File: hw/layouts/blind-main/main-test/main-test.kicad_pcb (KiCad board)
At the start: 2 copper layers, 148 parts

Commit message: Integrate regenerative clamp, thermal inhibit and priced component capture
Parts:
- added C55: , SAMSUNG_CL05B104KB54PNC:C0402, F.Cu at (880.0, 0.00)
- added C56: , SAMSUNG_CL05B104KB54PNC:C0402, F.Cu at (460.0, 0.00)
- added C57: , SAMSUNG_CL05B104KB54PNC:C0402, F.Cu at (450.0, 0.00)
- added C58: , SAMSUNG_CL05B104KB54PNC:C0402, F.Cu at (440.0, 0.00)
- added C59: , blind-supervisor:C0402, F.Cu at (370.0, 0.00)
- added C60: , SAMSUNG_CL05B104KB54PNC:C0402, F.Cu at (430.0, 0.00)
- added Q10: , blind-power:SOT-23-3_L2.9-W1.3-P1.90-LS2.4-BR, F.Cu at (0.00, 0.00)
- added Q4: , blind-power:SOT-23-3_L2.9-W1.3-P1.90-LS2.4-BR, F.Cu at (970.0, 0.00)
- added Q5: , blind-power:SOT-23-3_L2.9-W1.3-P1.90-LS2.4-BR, F.Cu at (680.0, 0.00)
- added Q6: , blind-carrier:PDFN-8_L3.3-W3.3-P0.65-BL, F.Cu at (730.0, 0.00)
- added Q7: , blind-power:SOT-23-3_L2.9-W1.3-P1.90-LS2.4-BR, F.Cu at (980.0, 0.00)
- added Q8: , blind-power:SOT-23-3_L2.9-W1.3-P1.90-LS2.4-BR, F.Cu at (920.0, 0.00)
- added Q9: , blind-carrier:PDFN-8_L3.3-W3.3-P0.65-BL, F.Cu at (740.0, 0.00)
- added R69: , blind-regen:R2512, F.Cu at (790.0, 0.00)
- added R70: , blind-regen:R2512, F.Cu at (800.0, 0.00)
- added R71: , blind-regen:R2512, F.Cu at (810.0, 0.00)
- added R72: , blind-regen:R2512, F.Cu at (820.0, 0.00)
- added R73: , blind-regen:R2512, F.Cu at (830.0, 0.00)
- added R74: , blind-regen:R2512, F.Cu at (840.0, 0.00)
- added R75: , blind-regen:R0603, F.Cu at (660.0, 0.00)
- added R76: , blind-regen:R0603, F.Cu at (670.0, 0.00)
- added R77: , blind-control-io:R0402, F.Cu at (710.0, 0.00)
- added R78: , blind-control-io:R0402, F.Cu at (720.0, 0.00)
- added R79: , UNI_ROYAL_0402WGF1002TCE:R0402, F.Cu at (930.0, 0.00)
- added R80: , UNI_ROYAL_0402WGF1002TCE:R0402, F.Cu at (940.0, 0.00)
- added R81: , blind-control-io:R0402, F.Cu at (890.0, 0.00)
- added R82: , blind-control-io:R0402, F.Cu at (760.0, 0.00)
- added R83: , UNI_ROYAL_0402WGF1002TCE:R0402, F.Cu at (910.0, 0.00)
- added R84: , blind-regen:R0402, F.Cu at (750.0, 0.00)
- added R85: , UNI_ROYAL_0402WGF1002TCE:R0402, F.Cu at (650.0, 0.00)
- added R86: , blind-regen:R0402, F.Cu at (630.0, 0.00)
- added R87: , UNI_ROYAL_0402WGF1002TCE:R0402, F.Cu at (640.0, 0.00)
- added R88: , blind-control-io:R0402, F.Cu at (960.0, 0.00)
- added R89: , UNI_ROYAL_0402WGF1002TCE:R0402, F.Cu at (380.0, 0.00)
- added R90: , UNI_ROYAL_0402WGF1002TCE:R0402, F.Cu at (410.0, 0.00)
- added R91: , blind-control-io:R0402, F.Cu at (420.0, 0.00)
- added R92: , UNI_ROYAL_0402WGF1002TCE:R0402, F.Cu at (390.0, 0.00)
- added R93: , UNI_ROYAL_0402WGF1002TCE:R0402, F.Cu at (400.0, 0.00)
- added U14: , blind-control-io:SOT-363_L2.0-W1.3-P0.65-LS2.1-BR, F.Cu at (350.0, 0.00)
- added U15: , blind-supervisor:SOT-23-6_L2.9-W1.6-P0.95-LS2.8-BR, F.Cu at (340.0, 0.00)
- added U16: , blind-supervisor:VSON-10_L3.0-W3.0-P0.50-TL-EP, F.Cu at (330.0, 0.00)
- added U17: , blind-supervisor:SC-70-6_L2.0-W1.3-P0.65-LS2.1-BR, F.Cu at (990.0, 0.00)
- C24: footprint blind-power:C0805 -> SAMSUNG_CL05B104KB54PNC:C0402
- C25, C39: footprint SAMSUNG_CL05B104KB54PNC:C0402 -> blind-power:C0805
- C30: footprint blind-core:CAP-SMD_BD6.3-L6.6-W6.6-LS7.3-FD -> SAMSUNG_CL05B104KB54PNC:C0402
- C31: footprint blind-core:C0402 -> blind-core:CAP-SMD_BD6.3-L6.6-W6.6-LS7.3-FD
- C32: footprint SAMSUNG_CL05B104KB54PNC:C0402 -> blind-core:C0402
- C38: footprint blind-supervisor:C0402 -> SAMSUNG_CL05B104KB54PNC:C0402
- R39, R40: footprint UNI_ROYAL_0402WGF1002TCE:R0402 -> blind-control-io:R0402
- R42, R43: footprint UNI_ROYAL_0402WGF1002TCE:R0402 -> blind-regen:R2512
- U5: footprint blind-supervisor:SC-70-6_L2.0-W1.3-P0.65-LS2.1-BR -> blind-regen:TSOT-23-6_L2.9-W1.6-P0.95-LS2.8-BR
- U6: footprint blind-control-io:SOT-363_L2.0-W1.3-P0.65-LS2.1-BR -> blind-regen:SOT-23-5_L3.0-W1.7-P0.95-LS2.8-BR
- U7: footprint blind-supervisor:SOT-23-6_L2.9-W1.6-P0.95-LS2.8-BR -> blind-regen:SOT-5X3-6_W1.6-L1.2-P0.50-LS1.6-BL
- U8: footprint blind-supervisor:VSON-10_L3.0-W3.0-P0.50-TL-EP -> blind-supervisor:SC-70-6_L2.0-W1.3-P0.65-LS2.1-BR
- moved C23 690.0 mm to (1010.0, 0.00)
- moved R39 620.0 mm to (1000.0, 0.00)
- moved U7 560.0 mm to (900.0, 0.00)
- moved C37 510.0 mm to (950.0, 0.00)
- moved U6 500.0 mm to (850.0, 0.00)
- moved C38 490.0 mm to (860.0, 0.00)
- moved C39 440.0 mm to (870.0, 0.00)
- moved R42 380.0 mm to (770.0, 0.00)
- moved R43 380.0 mm to (780.0, 0.00)
- moved C24 310.0 mm to (320.0, 0.00)
- moved R40 280.0 mm to (690.0, 0.00)
- moved R41 280.0 mm to (700.0, 0.00)
- moved C30 260.0 mm to (250.0, 0.00)
- moved U5 250.0 mm to (610.0, 0.00)
- moved C26 240.0 mm to (20.0, 0.00)
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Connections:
- net control-1 renamed controller-1
- net control-1-1 renamed controller-1-1
- net control-1-2 renamed controller-1-2
- net control-1-3 renamed controller-1-3
- net control.controller.mcu-4 renamed controller.mcu-4
- net nFAULT renamed D
- net usb_dn renamed usb_dm
- C23 pad 1: c_adc-1 -> rail-hv
- C24 pad 1: rail-hv -> c_adc-1
- C26 pad 1: c_down-1 -> rail-hv
- C27 pad 1: rail-hv -> c_down-1
- C28 pad 1: control.controller-2 -> rail-hv
- C29 pad 1: c_up-1 -> controller-2
- C30 pad 1: hv -> c_up-1
- C31 pad 1: CPH -> hv
- C31 pad 2: CPL -> lv
- C32 pad 1: VCP -> CPH
- C32 pad 2: hv -> CPL
- C33 pad 1: c_ref-1 -> VCP
- C33 pad 2: lv -> hv
- C34 pad 1: hv -> c_ref-1
- C35 pad 1: rail-hv -> hv
- C36 pad 1: rail-hv -> hv
- C37 pad 1: rail-hv -> c_hot_filter-1
- C37 pad 2: lv -> regen-2
- C38 pad 1: CWD -> hv
- C39 pad 1: rail-hv -> c_hot_filter-1
- R25 pad 2: control.controller-2 -> controller-2
- R26 pad 2: control.controller-2 -> controller-2
- R38 pad 1: motor_sleep_n-1 -> Y
- R39 pad 1: rail-hv -> Y
- R39 pad 2: motor_request_n-line -> lv
- R40 pad 1: rail-hv -> OUTB
- R40 pad 2: reset_n -> regen-2-2
- R41 pad 1: motor_sleep_n-1 -> hv
- R41 pad 2: lv -> regen-2-2
- R42 pad 1: rail-hv -> hv
- R42 pad 2: heartbeat-line -> r_dump1a-1
- R43 pad 1: rail-hv -> r_dump1a-1
- R43 pad 2: MR -> regen-2-1
- U3 pad 26: control.controller-2 -> controller-2
- U4 pad 3: motor_sleep_n-1 -> Y
- U5 pad 1: reset_n -> OUTA
- U5 pad 4: motor_sleep_n-1 -> threshold
- U5 pad 5: rail-hv -> hv
- U5 pad 6: control.supervision-6 -> OUTB
- U6 pad 1: motor_request_n-line -> hv
- U6 pad 3: heartbeat-line -> regen.thermal_supply-EN
- U6 pad 4: WDI -> regen.thermal_supply-NC
- U6 pad 5: rail-hv -> c_hot_filter-1
- U7 pad 1: reset_n -> c_hot_filter-1
- U7 pad 3: MR -> thermal_ok
- U7 pad 4: CT -> c_hot_filter-1
- U7 pad 5: rail-hv -> c_hot_filter-1
- U7 pad 6: rail-hv -> c_hot_filter-1
- U8 pad 1: rail-hv -> reset_n
- U8 pad 2: CWD -> lv
- U8 pad 3: control.supervision-6 -> lv
- U8 pad 4: CRST -> motor_sleep_n-Y
- U8 pad 5: lv -> rail-hv
- U8 pad 6: lv -> supervision-6

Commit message: Correct USB connector lands and document PD factory policy evidence
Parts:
- USBC1: footprint UNKNOWN_TYPE_C_31_M_12:USB-C_SMD-TYPE-C-31-M-12_1 -> blind-usb:HRO_TYPE_C_31_M_12

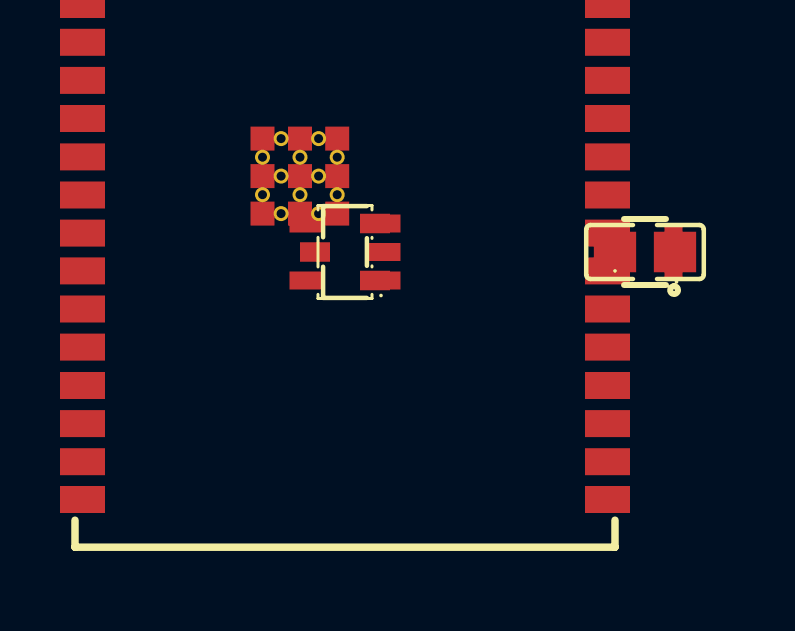
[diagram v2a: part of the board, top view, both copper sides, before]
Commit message: Connect protected pack and add gated C6 motion hardware adapter
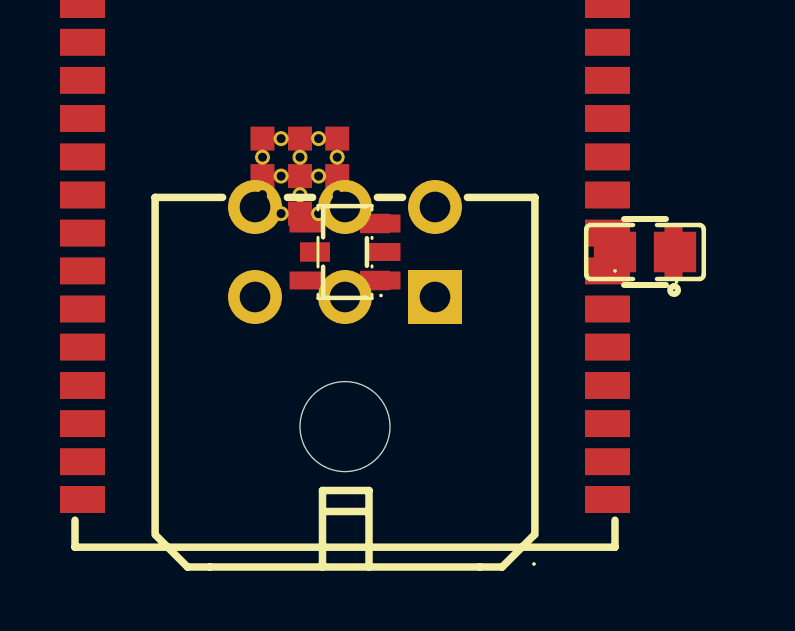
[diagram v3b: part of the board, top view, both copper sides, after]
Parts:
- added J1: , blind-connectors:CONN-TH_43045-0600, F.Cu at (0.00, 0.00)
